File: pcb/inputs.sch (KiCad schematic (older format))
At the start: 82 parts, among them P90 5v, P92 GND, P93 MAP, U11 MPXA6115AC6U, U4 MAX9926UAEE+, U6 MPXA4250AC6U

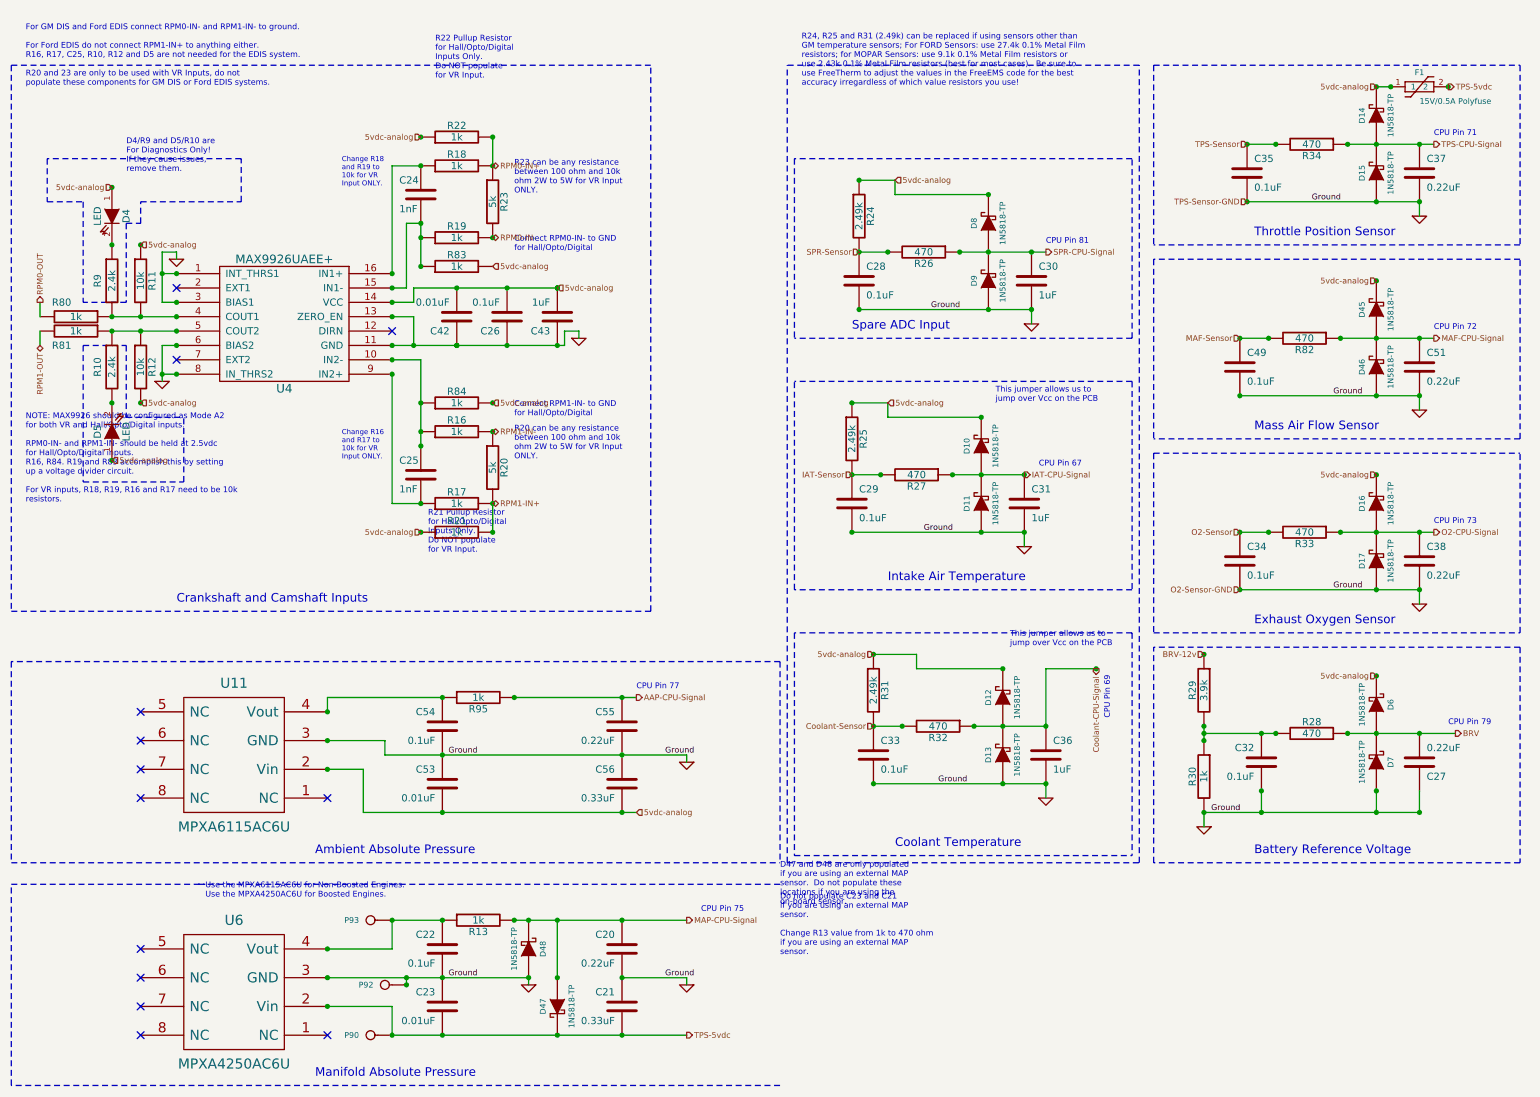
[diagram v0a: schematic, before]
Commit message: Added a second fuse (F2) between stock MAP power supply pad and external through hole 5vdc connection point for the external MAP sensor.
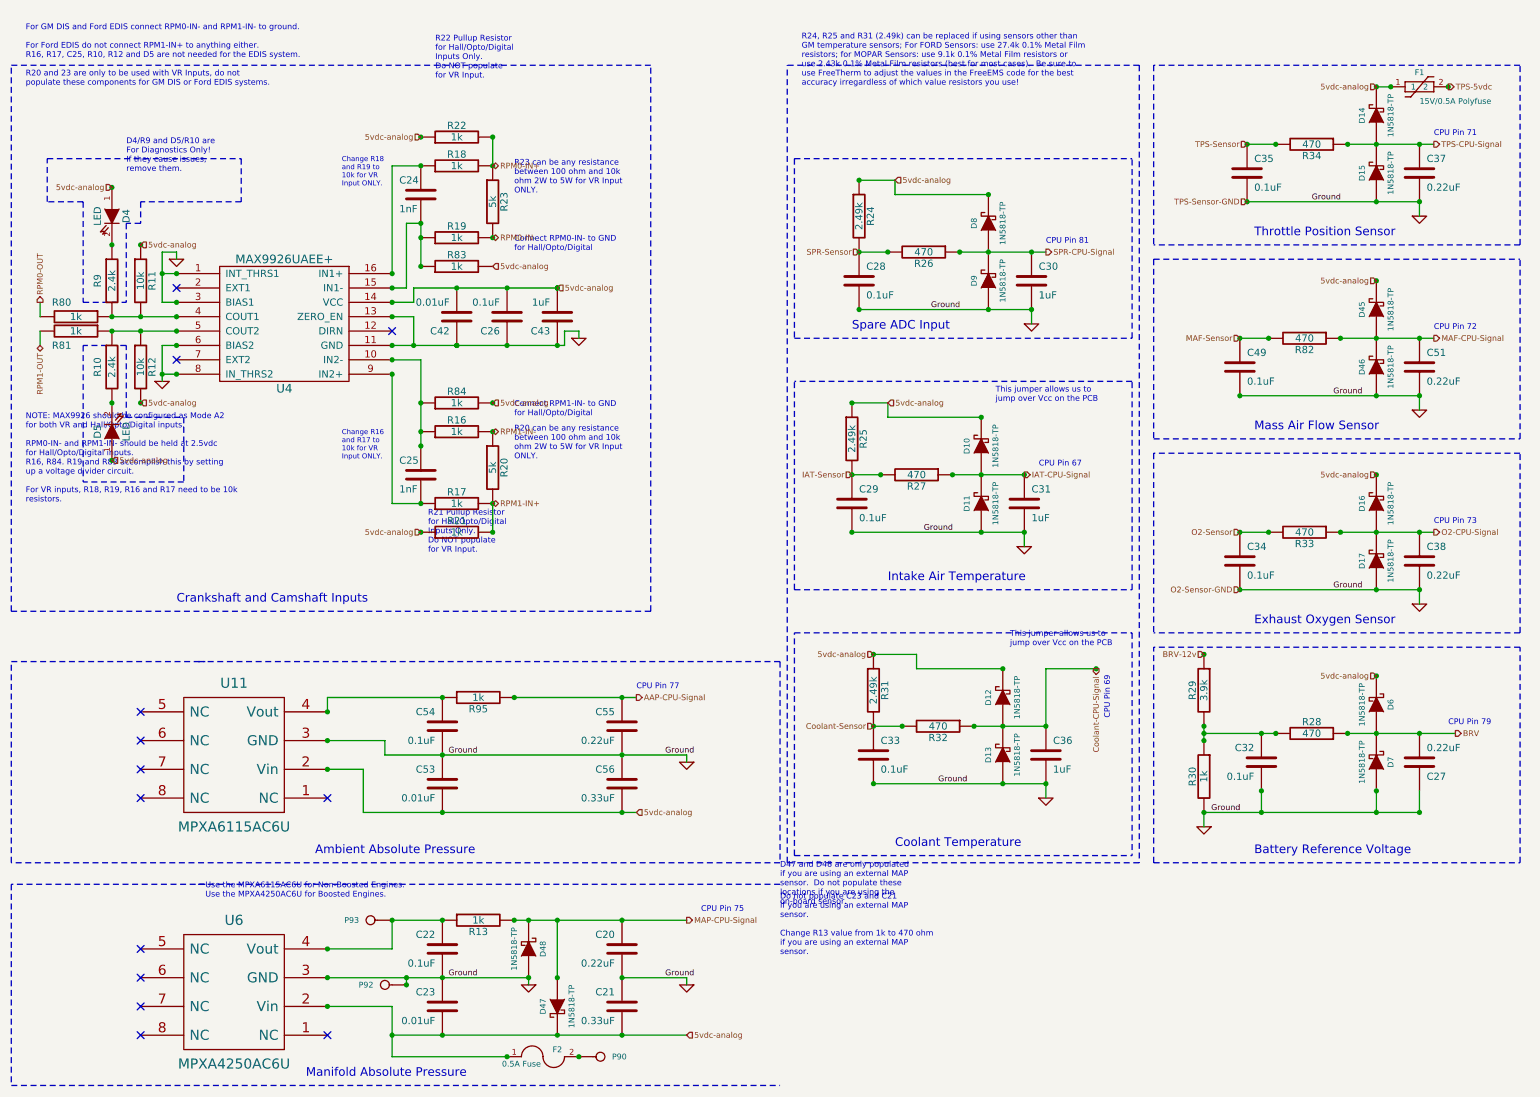
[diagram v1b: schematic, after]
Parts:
- added F2: 0.5A Fuse, symbol FUSE
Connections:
- net 5vdc-analog: now also C21.2, C23.2, D47.2 (K), U6.2 (Vin), F2.1
- net TPS-5vdc: no longer C21.2, C23.2, D47.2 (K), P90.1, U6.2 (Vin)
- new net: F2.2, P90.1
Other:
- moved on the sheet: P90

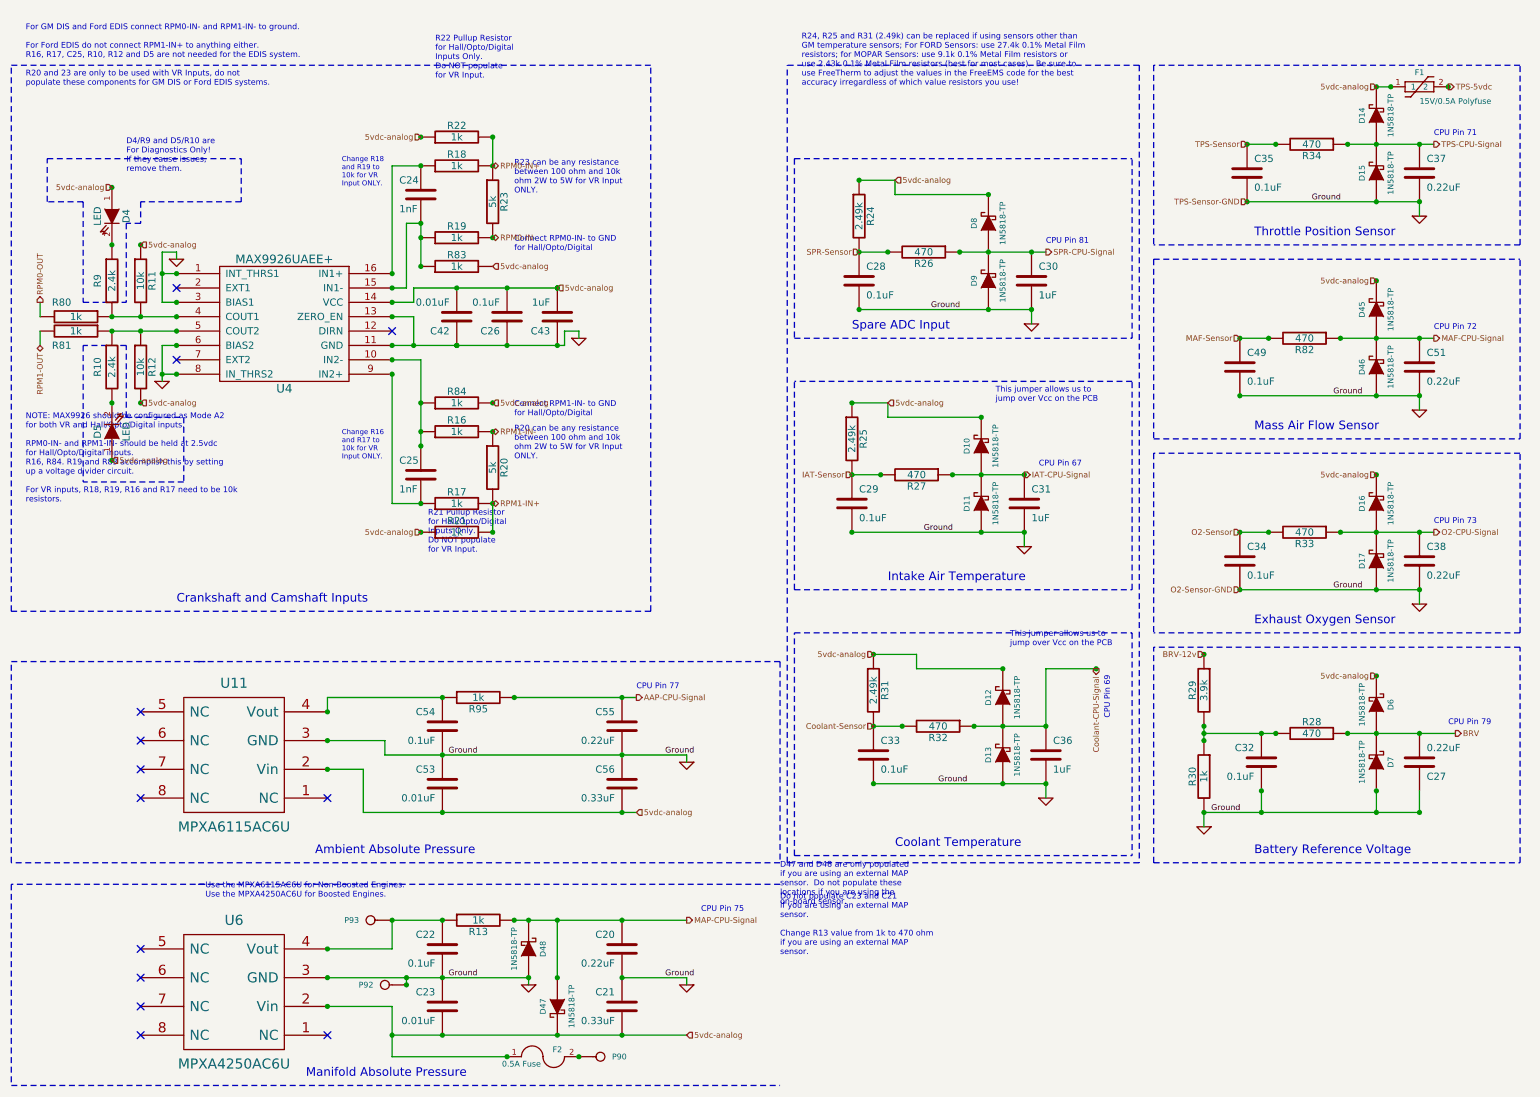
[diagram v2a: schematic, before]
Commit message: Cleaned up notes on the Inputs schematic page to remove notes about jumpers that are not needed.
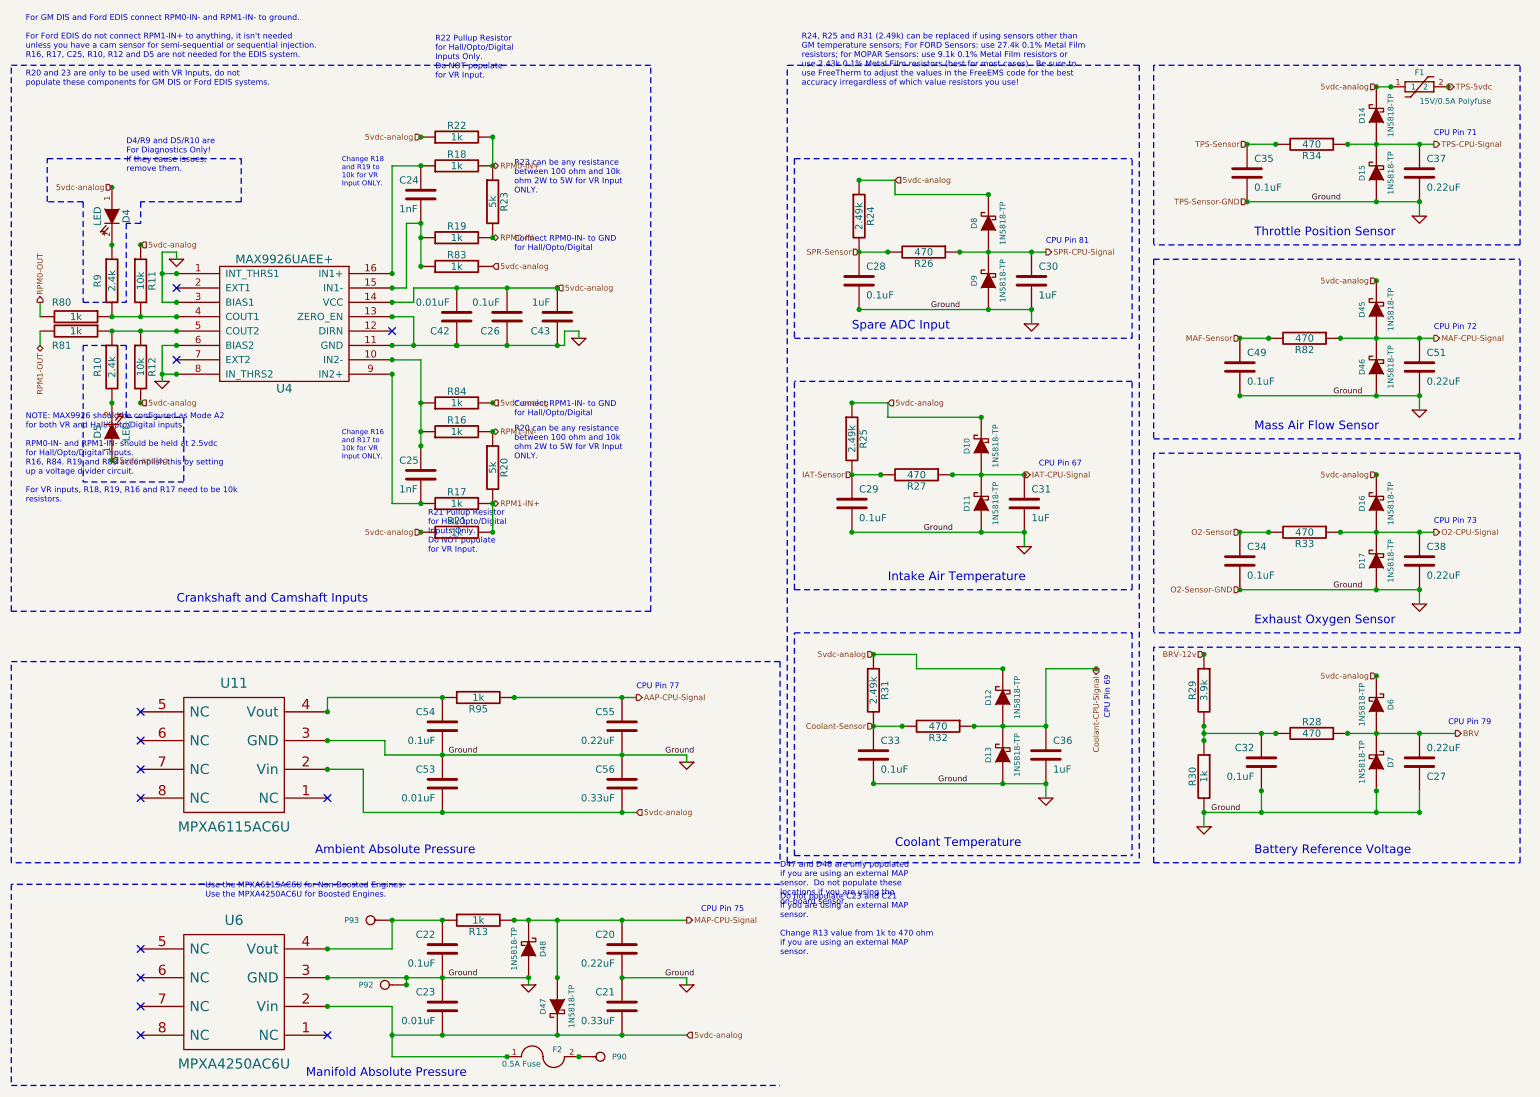
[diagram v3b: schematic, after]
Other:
- note added: "For GM DIS and Ford EDIS connect RPM0-IN- and RPM1-IN- to ground.\n\nFor Ford EDIS do not connect RPM1-IN+ to anything, it isn't needed\nunless you have a cam sensor for semi-sequential or sequential injection. \nR16, R17, C25, R10, R12 and D5 are not needed for the EDIS system.\n\nR20 and 23 are only to be used with VR Inputs, do not\npopulate these components for GM DIS or Ford EDIS systems."
- note removed: "For GM DIS and Ford EDIS connect RPM0-IN- and RPM1-IN- to ground.\n\nFor Ford EDIS do not connect RPM1-IN+ to anything either. \nR16, R17, C25, R10, R12 and D5 are not needed for the EDIS system.\n\nR20 and 23 are only to be used with VR Inputs, do not\npopulate these components for GM DIS or Ford EDIS systems."
- note removed: "This jumper allows us to \njump over Vcc on the PCB"
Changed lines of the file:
@@
-EESchema Schematic File Version 2  date Tue 21 May 2013 08:16:12 PM EDT
+EESchema Schematic File Version 2  date Thu 23 May 2013 09:51:59 PM EDT
 LIBS:opto
 LIBS:power
@@
 Sheet 4 7
 Title "Jaguar PCB for FreeEMS"
-Date "22 may 2013"
+Date "24 may 2013"
 Rev "0.6-alpha"
 Comp "git hash: xxxxxxxxxx"
@@
 R24, R25 and R31 (2.49k) can be replaced if using sensors other than\nGM temperature sensors; For FORD Sensors: use 27.4k 0.1% Metal Film\nresistors; for MOPAR Sensors: use 9.1k 0.1% Metal Film resistors or \nuse 2.43k 0.1% Metal Film resistors (best for most cases).  Be sure to\nuse FreeTherm to adjust the values in the FreeEMS code for the best\naccuracy irregardless of which value resistors you use!
 Text Notes 650  750  0    40   ~ 0
-For GM DIS and Ford EDIS connect RPM0-IN- and RPM1-IN- to ground.\n\nFor Ford EDIS do not connect RPM1-IN+ to anything either. \nR16, R17, C25, R10, R12 and D5 are not needed for the EDIS system.\n\nR20 and 23 are only to be used with VR Inputs, do not\npopulate these components for GM DIS or Ford EDIS systems.
+For GM DIS and Ford EDIS connect RPM0-IN- and RPM1-IN- to ground.\n\nFor Ford EDIS do not connect RPM1-IN+ to anything, it isn't needed\nunless you have a cam sensor for semi-sequential or sequential injection. \nR16, R17, C25, R10, R12 and D5 are not needed for the EDIS system.\n\nR20 and 23 are only to be used with VR Inputs, do not\npopulate these components for GM DIS or Ford EDIS systems.
 Text Notes 1350 1350 0    40   ~ 0
 D4/R9 and D5/R10 are \nFor Diagnostics Only!\nIf they cause issues, \nremove them.
@@
 	1    0    0    -1
 $EndComp
-Text Notes 7500 4650 0    40   ~ 0
-This jumper allows us to \njump over Vcc on the PCB
-Text Notes 7400 2950 0    40   ~ 0
-This jumper allows us to \njump over Vcc on the PCB
 $Comp
 L GND #PWR027

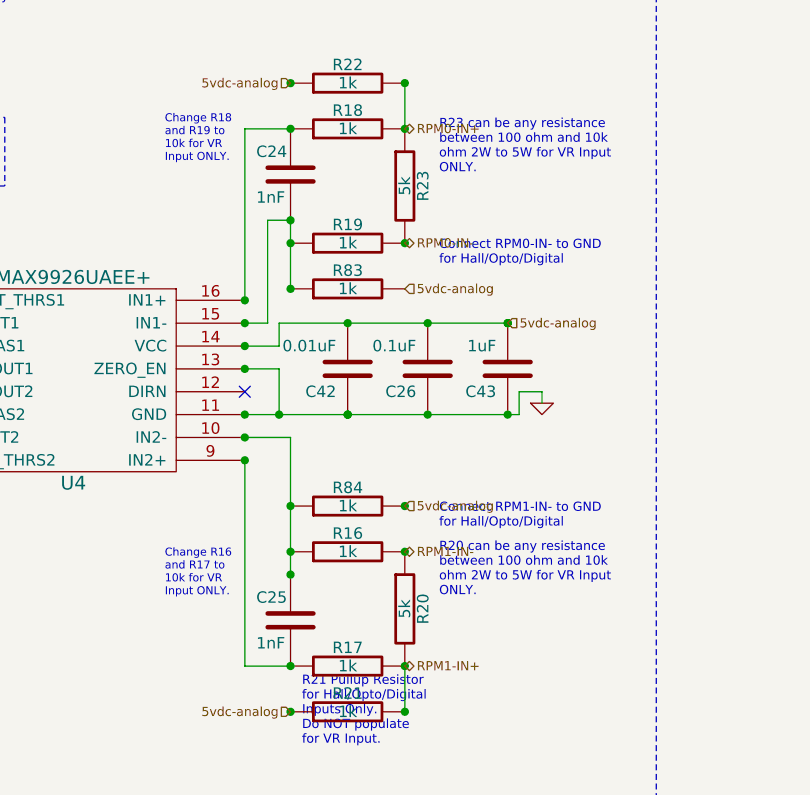
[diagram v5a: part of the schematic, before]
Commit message: Changed VR shunt resistors (R20 and R23) from 5k to 5.1k due to 2W package availability.
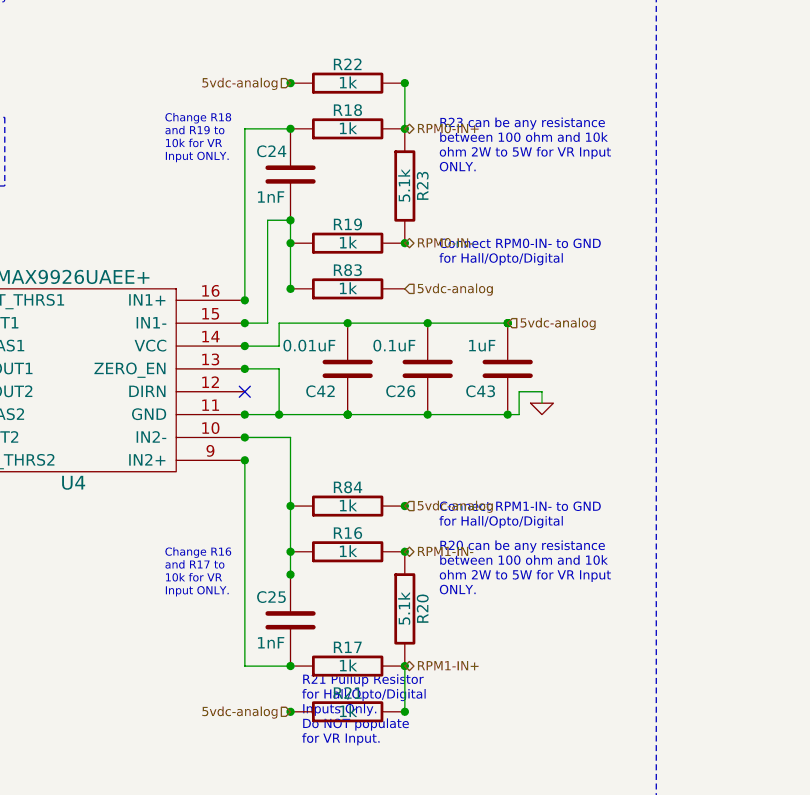
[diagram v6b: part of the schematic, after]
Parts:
- R20, R23: value 5k -> 5.1k
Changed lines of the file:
@@
-EESchema Schematic File Version 2  date Fri 24 May 2013 09:31:09 PM EDT
+EESchema Schematic File Version 2  date Fri 24 May 2013 09:46:28 PM EDT
 LIBS:opto
 LIBS:power
@@
 P 3900 3400
 F 0 "R20" V 3980 3400 50  0000 C CNN
-F 1 "5k" V 3900 3400 50  0000 C CNN
+F 1 "5.1k" V 3900 3400 50  0000 C CNN
 	1    3900 3400
 	1    0    0    -1
@@
 P 3900 1550
 F 0 "R23" V 3980 1550 50  0000 C CNN
-F 1 "5k" V 3900 1550 50  0000 C CNN
+F 1 "5.1k" V 3900 1550 50  0000 C CNN
 	1    3900 1550
 	1    0    0    -1
